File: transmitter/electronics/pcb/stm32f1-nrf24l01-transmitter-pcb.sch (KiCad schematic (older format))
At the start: 34 parts, among them K1 CONN_3, K10 CONN_3, K11 CONN_3, K12 UART, K2 CONN_3, K3 CONN_3, K4 CONN_3, K5 CONN_3, K6 CONN_3, K7 CONN_3, K8 CONN_3, K9 CONN_3, P1 Charge, P2 LED, P3 PWR-BAT, P4 PWR-IN, P5 Buzzer, P6 Meter, Q1 BC547B, SW1 ON/OFF, U1 LIPO_CHARGER_+_PROTECTION, U2 STM32F103C8T6_DEV_BOARD, U3 NRF24L01P

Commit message: Work on PCB
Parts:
- removed BT1: BATTERY, Pin_Headers:Pin_Header_Straight_1x02_Pitch2.54mm, symbol stm32f1-nrf24l01-transmitter-rescue:BATTERY
- removed P1: Charge, Pin_Headers:Pin_Header_Straight_1x02_Pitch2.54mm, symbol stm32f1-nrf24l01-transmitter-rescue:CONN_2
- removed P3: PWR-BAT, Pin_Headers:Pin_Header_Straight_1x02_Pitch2.54mm, symbol stm32f1-nrf24l01-transmitter-rescue:CONN_2
- removed P4: PWR-IN, Pin_Headers:Pin_Header_Straight_1x02_Pitch2.54mm, symbol stm32f1-nrf24l01-transmitter-rescue:CONN_2
- removed SW1: ON/OFF, Buttons_Switches_SMD:SW_SPST_FSMSM, symbol stm32f1-nrf24l01-transmitter-rescue:SPST
- added H1, H2: MountingHole, MountingHole:MountingHole_3.2mm_M3_DIN965, symbol Mechanical:MountingHole
- added J12: PB5, Connector_JST:JST_EH_B3B-EH-A_1x03_P2.50mm_Vertical, symbol stm32f1-nrf24l01-transmitter-rescue:CONN_3
- added J13: PB6, Connector_JST:JST_EH_B3B-EH-A_1x03_P2.50mm_Vertical, symbol stm32f1-nrf24l01-transmitter-rescue:CONN_3
- added J14: PB7, Connector_JST:JST_EH_B3B-EH-A_1x03_P2.50mm_Vertical, symbol stm32f1-nrf24l01-transmitter-rescue:CONN_3
- added J15: PB8, Connector_JST:JST_EH_B3B-EH-A_1x03_P2.50mm_Vertical, symbol stm32f1-nrf24l01-transmitter-rescue:CONN_3
- added J16: PB10, Connector_JST:JST_EH_B3B-EH-A_1x03_P2.50mm_Vertical, symbol stm32f1-nrf24l01-transmitter-rescue:CONN_3
- added J17: PB11, Connector_JST:JST_EH_B3B-EH-A_1x03_P2.50mm_Vertical, symbol stm32f1-nrf24l01-transmitter-rescue:CONN_3
- added J18: USB, Connector_JST:JST_EH_B4B-EH-A_1x04_P2.50mm_Vertical, symbol Connector_Generic:Conn_01x04
- added J19: BATTERY, Connector_JST:JST_EH_B2B-EH-A_1x02_P2.50mm_Vertical, symbol Connector_Generic:Conn_01x02
- added J21: SWITCH, Connector_JST:JST_EH_B2B-EH-A_1x02_P2.50mm_Vertical, symbol Connector_Generic:Conn_01x02
- added J22: NRF24 connector, Connector_JST:JST_EH_B7B-EH-A_1x07_P2.50mm_Vertical, symbol Connector_Generic:Conn_01x07
- added J26: Red, TestPoint:TestPoint_Pad_1.5x1.5mm, symbol Connector_Generic:Conn_01x01
- added J27: Blue, TestPoint:TestPoint_Pad_1.5x1.5mm, symbol Connector_Generic:Conn_01x01
- added J28: Charger LED, Connector_JST:JST_EH_B3B-EH-A_1x03_P2.50mm_Vertical, symbol Connector_Generic:Conn_01x03
- C1: renamed from C2; footprint Capacitors_SMD:C_0805_HandSoldering -> Capacitor_SMD:C_0805_2012Metric_Pad1.15x1.40mm_HandSolder
- C2: renamed from C3; footprint Capacitors_SMD:C_0805_HandSoldering -> Capacitor_SMD:C_0805_2012Metric_Pad1.15x1.40mm_HandSolder
- C3: renamed from C4; footprint Capacitors_SMD:C_0805_HandSoldering -> Capacitor_SMD:C_0805_2012Metric_Pad1.15x1.40mm_HandSolder
- C4: renamed from C1; footprint Capacitors_SMD:C_0805_HandSoldering -> Capacitor_SMD:C_0805_2012Metric_Pad1.15x1.40mm_HandSolder
- J1: renamed from K1; value CONN_3 -> PA1/A1; footprint Pin_Headers:Pin_Header_Straight_1x03_Pitch2.54mm -> Connector_JST:JST_EH_B3B-EH-A_1x03_P2.50mm_Vertical
- J10: renamed from K10; value CONN_3 -> PB3; footprint Pin_Headers:Pin_Header_Straight_1x03_Pitch2.54mm -> Connector_JST:JST_EH_B3B-EH-A_1x03_P2.50mm_Vertical
- J11: renamed from K11; value CONN_3 -> PB4; footprint Pin_Headers:Pin_Header_Straight_1x03_Pitch2.54mm -> Connector_JST:JST_EH_B3B-EH-A_1x03_P2.50mm_Vertical
- J2: renamed from K2; value CONN_3 -> PA2/A2; footprint Pin_Headers:Pin_Header_Straight_1x03_Pitch2.54mm -> Connector_JST:JST_EH_B3B-EH-A_1x03_P2.50mm_Vertical
- J20: renamed from K12; footprint Pin_Headers:Pin_Header_Straight_1x03_Pitch2.54mm -> Connector_PinHeader_2.54mm:PinHeader_1x03_P2.54mm_Vertical; symbol stm32f1-nrf24l01-transmitter-rescue:CONN_3 -> Connector_Generic:Conn_01x03
- J23: renamed from P5; footprint Pin_Headers:Pin_Header_Straight_1x02_Pitch2.54mm -> Connector_JST:JST_EH_B2B-EH-A_1x02_P2.50mm_Vertical; symbol stm32f1-nrf24l01-transmitter-rescue:CONN_2 -> Connector_Generic:Conn_01x02
- J24: renamed from P6; footprint Pin_Headers:Pin_Header_Straight_1x02_Pitch2.54mm -> Connector_JST:JST_EH_B2B-EH-A_1x02_P2.50mm_Vertical; symbol stm32f1-nrf24l01-transmitter-rescue:CONN_2 -> Connector_Generic:Conn_01x02
- J25: renamed from P2; footprint Pin_Headers:Pin_Header_Straight_1x02_Pitch2.54mm -> Connector_JST:JST_EH_B2B-EH-A_1x02_P2.50mm_Vertical; symbol stm32f1-nrf24l01-transmitter-rescue:CONN_2 -> Connector_Generic:Conn_01x02
- J3: renamed from K3; value CONN_3 -> PA3/A3; footprint Pin_Headers:Pin_Header_Straight_1x03_Pitch2.54mm -> Connector_JST:JST_EH_B3B-EH-A_1x03_P2.50mm_Vertical
- J4: renamed from K4; value CONN_3 -> PA4/A4; footprint Pin_Headers:Pin_Header_Straight_1x03_Pitch2.54mm -> Connector_JST:JST_EH_B3B-EH-A_1x03_P2.50mm_Vertical
- J5: renamed from K5; value CONN_3 -> PA5/A5; footprint Pin_Headers:Pin_Header_Straight_1x03_Pitch2.54mm -> Connector_JST:JST_EH_B3B-EH-A_1x03_P2.50mm_Vertical
- J6: renamed from K6; value CONN_3 -> PA6/A6; footprint Pin_Headers:Pin_Header_Straight_1x03_Pitch2.54mm -> Connector_JST:JST_EH_B3B-EH-A_1x03_P2.50mm_Vertical
- J7: renamed from K7; value CONN_3 -> PA7/A7; footprint Pin_Headers:Pin_Header_Straight_1x03_Pitch2.54mm -> Connector_JST:JST_EH_B3B-EH-A_1x03_P2.50mm_Vertical
- J8: renamed from K8; value CONN_3 -> PB0/A8; footprint Pin_Headers:Pin_Header_Straight_1x03_Pitch2.54mm -> Connector_JST:JST_EH_B3B-EH-A_1x03_P2.50mm_Vertical
- J9: renamed from K9; value CONN_3 -> PB1/A9; footprint Pin_Headers:Pin_Header_Straight_1x03_Pitch2.54mm -> Connector_JST:JST_EH_B3B-EH-A_1x03_P2.50mm_Vertical
- Q1: footprint TO_SOT_Packages_THT:TO-92_Inline_Wide -> Package_TO_SOT_SMD:SOT-23_Handsoldering
- R1: renamed from R2; footprint Resistors_SMD:R_0805_HandSoldering -> Resistor_SMD:R_0805_2012Metric_Pad1.15x1.40mm_HandSolder
- R2: renamed from R3; footprint Resistors_SMD:R_0805_HandSoldering -> Resistor_SMD:R_0805_2012Metric_Pad1.15x1.40mm_HandSolder
- R3: renamed from R4; footprint Resistors_SMD:R_0805_HandSoldering -> Resistor_SMD:R_0805_2012Metric_Pad1.15x1.40mm_HandSolder
- R4: renamed from R5; footprint Resistors_SMD:R_0805_HandSoldering -> Resistor_SMD:R_0805_2012Metric_Pad1.15x1.40mm_HandSolder
- R5: renamed from R1; footprint Resistors_SMD:R_0805_HandSoldering -> Resistor_SMD:R_0805_2012Metric_Pad1.15x1.40mm_HandSolder
- SP1: footprint Buzzers_Beepers:Buzzer_12x9.5RM7.6 -> Buzzer_Beeper:Buzzer_12x9.5RM7.6
- U2: footprint WLA:STM32F103C8T6 -> WLA:STM32F103C8T6_DEV_BOARD
- U3: footprint WLA:NRF24L01P-PA-LNA -> Connector_PinHeader_2.54mm:PinHeader_2x04_P2.54mm_Vertical
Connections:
- net BUZZER: now also R3.2; no longer R3.1
- net CSN: now also J22.3 (Pin_3)
- net GND: now also J12.1 (P1), J13.1 (P1), J14.1 (P1), J15.1 (P1), J16.1 (P1), J17.1 (P1), J18.1 (Pin_1), J22.1 (Pin_1)
- net IRQ: now also J22.5 (Pin_5)
- net MISO: now also J22.6 (Pin_6)
- net MOSI: now also J22.4 (Pin_4)
- net PB10: now also J16.3 (P3); no longer J11.3 (P3)
- net PB11: now also J17.3 (P3); no longer J10.3 (P3)
- net PB3: now also J10.3 (P3)
- net PB4: now also J11.3 (P3)
- net PB5: now also J12.3 (P3)
- net PB6: now also J13.3 (P3)
- net PB7: now also J14.3 (P3)
- net PB8: now also J15.3 (P3)
- net RX: now also J20.3 (Pin_3); no longer J20.2 (PM)
- net SCK: now also J22.7 (Pin_7)
- net TX: now also J20.2 (Pin_2); no longer J20.3 (P3)
- net VCC: now also J12.2 (PM), J13.2 (PM), J14.2 (PM), J15.2 (PM), J16.2 (PM), J17.2 (PM), J22.2 (Pin_2)
- net VDD: now also J21.2 (Pin_2)
- net USBDM: now reaches U2.8 (PA11/USBDM)
- net USBDM: now also J18.3 (Pin_3)
- net USBDP: now reaches U2.9 (PA12/USBDP)
- net USBDP: now also J18.2 (Pin_2)
- net at U1.1 (LiPo+): now also J19.2 (Pin_2)
- net at U1.2 (LiPo-): now also J19.1 (Pin_1)
- net at U1.3 (OUT+): now also J21.1 (Pin_1)
- net +USB: now reaches U1.5 (USB+)
- net +USB: now also J18.4 (Pin_4), J28.3 (Pin_3)
- net at Q1.2 (B): now also R3.1; no longer R3.2
- net PB9 renamed METER
- new net: J27.1 (Pin_1), J28.1 (Pin_1)
- new net: J26.1 (Pin_1), J28.2 (Pin_2)
- no-connect marks 11 -> 3
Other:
- note added: "Note that 4 pins of J22 and U3 are \nmade to overlap, so that we can save \nspace since we only want one \noption ever"
- note added: "USB"
- moved on the sheet: C1, C2, C3, C4, Q1, R1, R2, R3, R4, R5, SP1, U1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

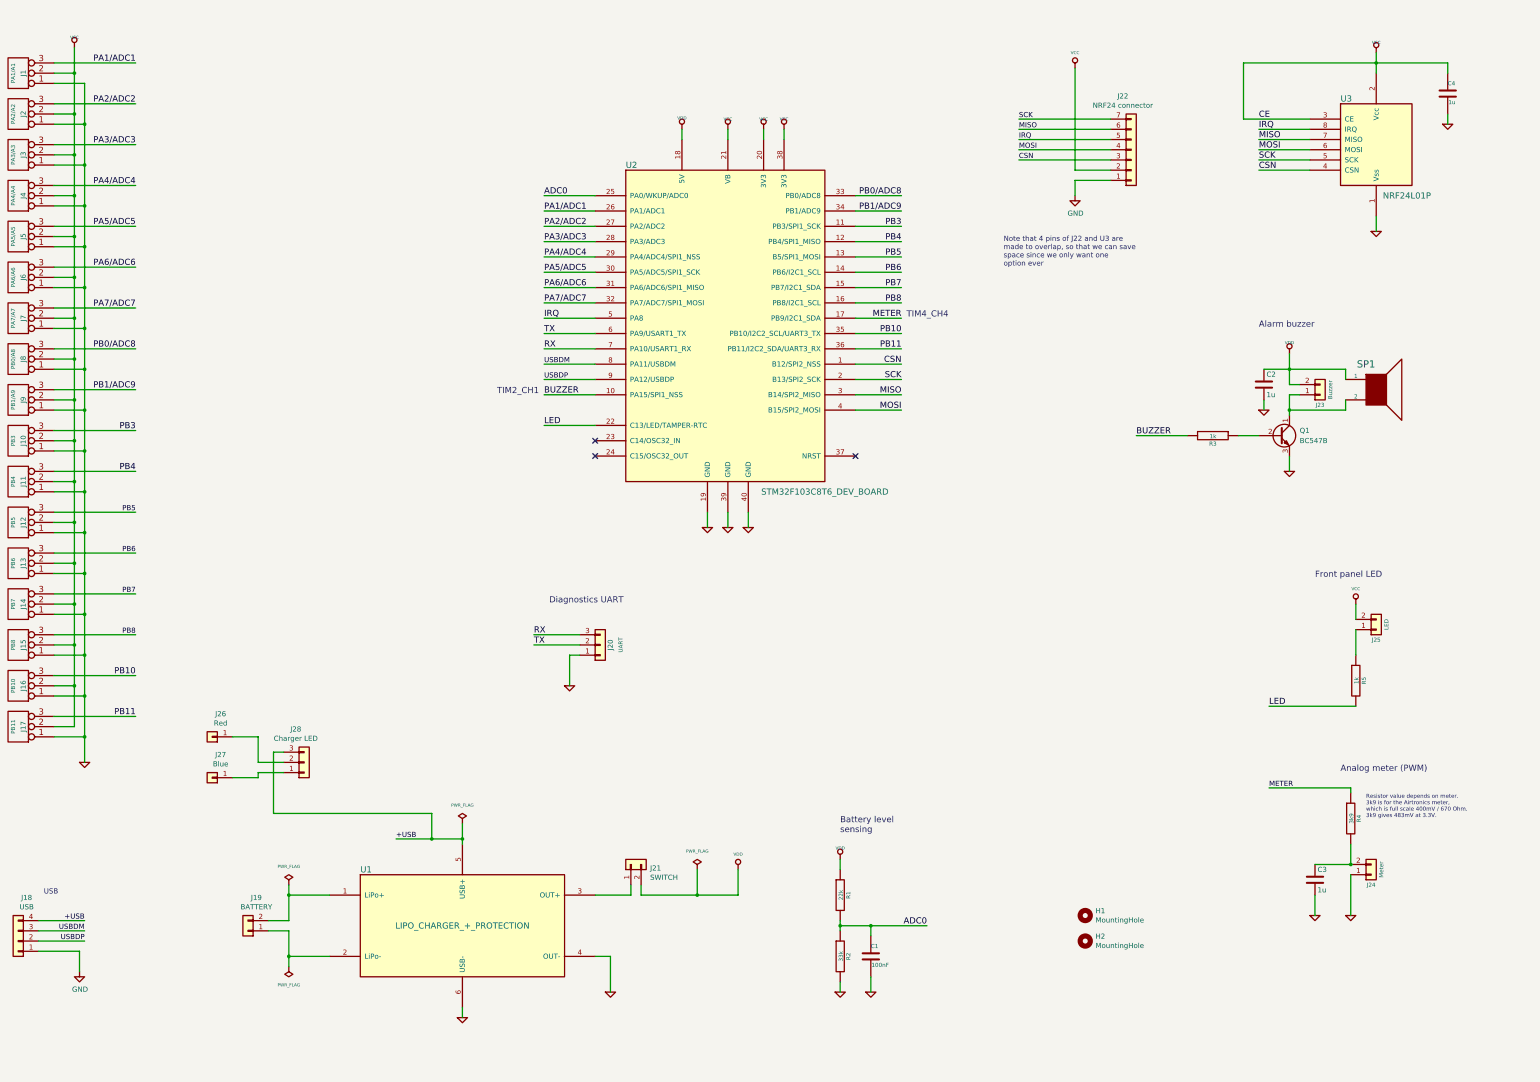
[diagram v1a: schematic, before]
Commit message: Update PCB without Blue Pill, but use STM32F103 directly
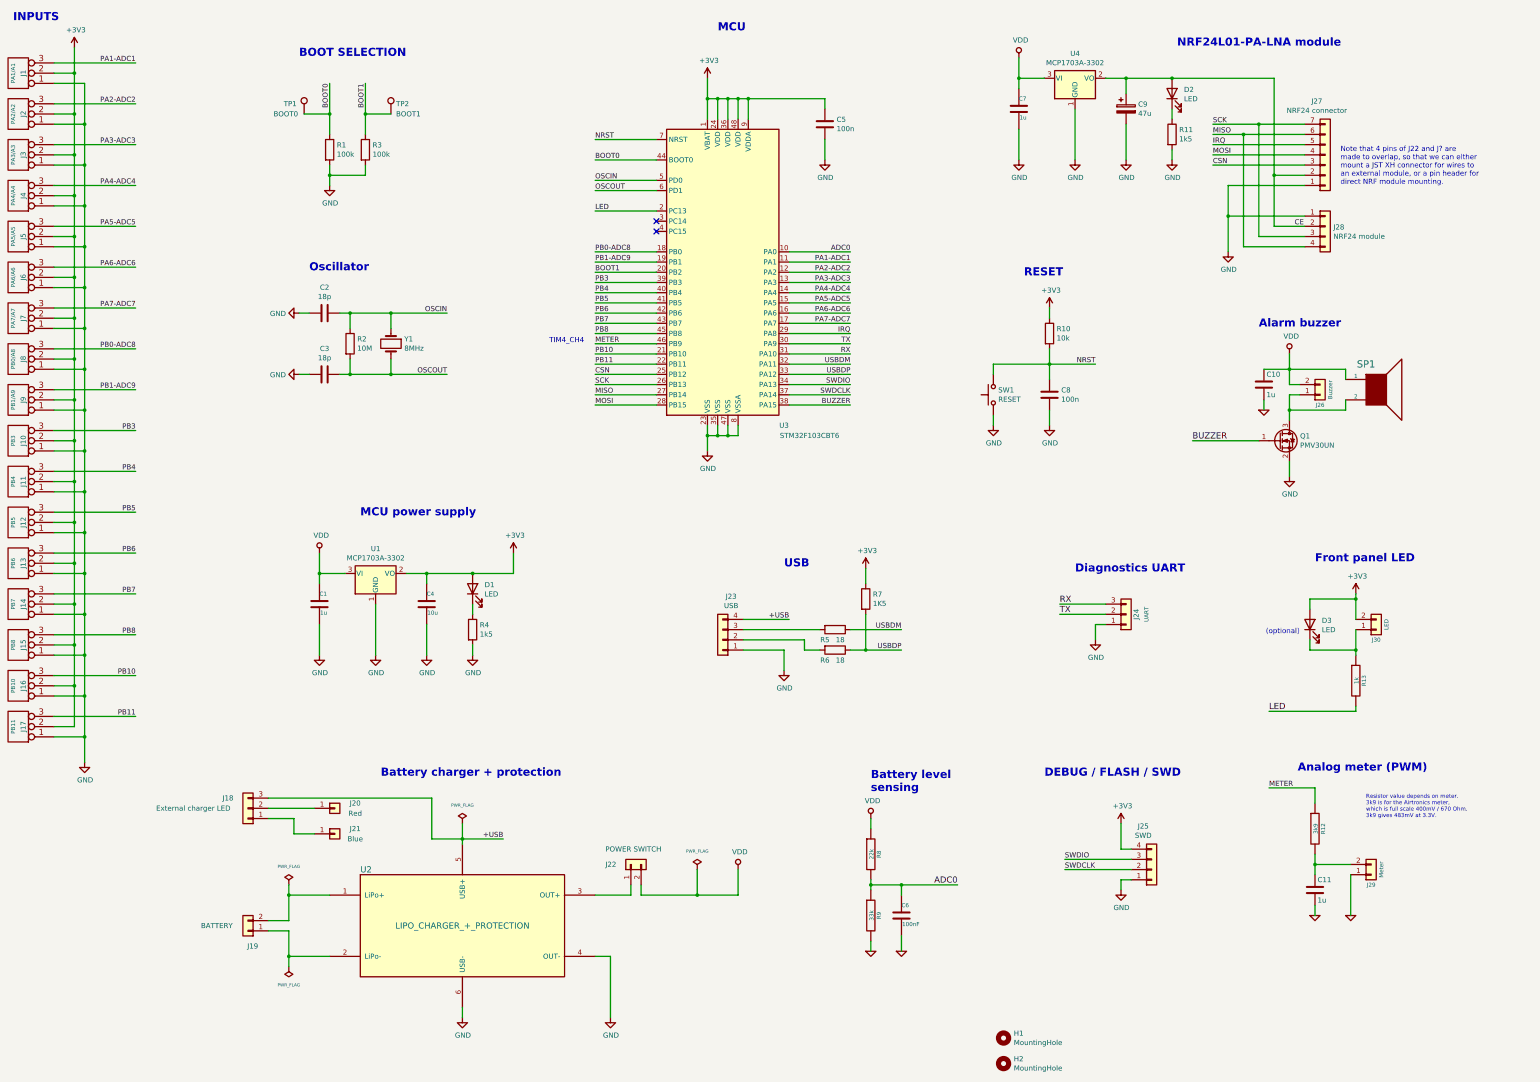
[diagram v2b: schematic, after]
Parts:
- removed Q1: BC547B, Package_TO_SOT_SMD:SOT-23_Handsoldering, symbol stm32f1-nrf24l01-transmitter-rescue:Q_NPN_CBE
- removed R3: 1k, Resistor_SMD:R_0805_2012Metric_Pad1.15x1.40mm_HandSolder, symbol stm32f1-nrf24l01-transmitter-rescue:R-RESCUE-stm32f1-nrf24l01-transmitter
- removed U2: STM32F103C8T6_DEV_BOARD, WLA:STM32F103C8T6_DEV_BOARD, symbol stm32f1-nrf24l01-transmitter-rescue:STM32F103C8T6_DEV_BOARD
- removed U3: NRF24L01P, Connector_PinHeader_2.54mm:PinHeader_2x04_P2.54mm_Vertical, symbol stm32f1-nrf24l01-transmitter-rescue:NRF24L01P
- added C1, C7: 1u, Capacitor_SMD:C_0805_2012Metric_Pad1.15x1.40mm_HandSolder, symbol stm32f1-nrf24l01-transmitter-rescue:C-RESCUE-stm32f1-nrf24l01-transmitter
- added C2, C3: 18p, Capacitor_SMD:C_0603_1608Metric_Pad1.05x0.95mm_HandSolder, symbol Device:C
- added C5, C8: 100n, Capacitor_SMD:C_0603_1608Metric_Pad1.05x0.95mm_HandSolder, symbol Device:C
- added C9: 47u, Capacitor_SMD:C_0805_2012Metric_Pad1.15x1.40mm_HandSolder, symbol Device:CP
- added D1, D2, D3: LED, LED_SMD:LED_0805_2012Metric_Pad1.15x1.40mm_HandSolder, symbol Device:LED
- added J25: SWD, Connector_PinHeader_2.54mm:PinHeader_1x04_P2.54mm_Vertical, symbol Connector_Generic:Conn_01x04
- added J28: NRF24 module, Connector_PinHeader_2.54mm:PinHeader_1x04_P2.54mm_Vertical, symbol Connector_Generic:Conn_01x04
- added Q1: PMV30UN, Package_TO_SOT_SMD:SOT-23, symbol Transistor_FET:BSS138
- added R1, R3: 100k, Resistor_SMD:R_0805_2012Metric_Pad1.15x1.40mm_HandSolder, symbol Device:R
- added R10: 10k, Resistor_SMD:R_0805_2012Metric_Pad1.15x1.40mm_HandSolder, symbol Device:R
- added R11, R4: 1k5, Resistor_SMD:R_0805_2012Metric_Pad1.15x1.40mm_HandSolder, symbol Device:R
- added R2: 10M, Resistor_SMD:R_0805_2012Metric_Pad1.15x1.40mm_HandSolder, symbol Device:R
- added R5, R6: 18, Resistor_SMD:R_0805_2012Metric_Pad1.15x1.40mm_HandSolder, symbol Device:R
- added R7: 1K5, Resistor_SMD:R_0805_2012Metric_Pad1.15x1.40mm_HandSolder, symbol Device:R
- added SW1: RESET, tact-switch:Tact switch 6x4x3, symbol Switch:SW_Push
- added TP1: BOOT0, TestPoint:TestPoint_Pad_1.5x1.5mm, symbol Connector:TestPoint
- added TP2: BOOT1, TestPoint:TestPoint_Pad_1.5x1.5mm, symbol Connector:TestPoint
- added U1, U4: MCP1703A-3302, Package_TO_SOT_SMD:SOT-23, symbol Regulator_Linear:MCP1703A-3302_SOT23
- added U3: STM32F103CBT6, Package_QFP:LQFP-48_7x7mm_P0.5mm, symbol MCU_ST_STM32F1:STM32F103CBTx
- added Y1: 8MHz, Crystal:Crystal_SMD_5032-2Pin_5.0x3.2mm_HandSoldering, symbol Device:Crystal
- C4: value 1u -> 10u
- J1, J10, J11, J12, J13, J14, J15, J16, J17, J2, J3, J4, J5, J6, J7, J8, J9: footprint Connector_JST:JST_EH_B3B-EH-A_1x03_P2.50mm_Vertical -> Connector_JST:JST_XH_B3B-XH-A_1x03_P2.50mm_Vertical
- J18: renamed from J28; value Charger LED -> External charger LED; footprint Connector_JST:JST_EH_B3B-EH-A_1x03_P2.50mm_Vertical -> Connector_JST:JST_XH_B3B-XH-A_1x03_P2.50mm_Vertical
- J19: footprint Connector_JST:JST_EH_B2B-EH-A_1x02_P2.50mm_Vertical -> Connector_JST:JST_XH_B2B-XH-A_1x02_P2.50mm_Vertical
- J22: renamed from J21; value SWITCH -> POWER SWITCH; footprint Connector_JST:JST_EH_B2B-EH-A_1x02_P2.50mm_Vertical -> Connector_JST:JST_XH_B2B-XH-A_1x02_P2.50mm_Vertical
- J23: renamed from J18; footprint Connector_JST:JST_EH_B4B-EH-A_1x04_P2.50mm_Vertical -> Connector_JST:JST_XH_B4B-XH-A_1x04_P2.50mm_Vertical
- J26: renamed from J23; footprint Connector_JST:JST_EH_B2B-EH-A_1x02_P2.50mm_Vertical -> Connector_JST:JST_XH_B2B-XH-A_1x02_P2.50mm_Vertical
- J27: renamed from J22; footprint Connector_JST:JST_EH_B7B-EH-A_1x07_P2.50mm_Vertical -> Connector_JST:JST_XH_B7B-XH-A_1x07_P2.50mm_Vertical
- J29: renamed from J24; footprint Connector_JST:JST_EH_B2B-EH-A_1x02_P2.50mm_Vertical -> Connector_JST:JST_XH_B2B-XH-A_1x02_P2.50mm_Vertical
- J30: renamed from J25; footprint Connector_JST:JST_EH_B2B-EH-A_1x02_P2.50mm_Vertical -> Connector_JST:JST_XH_B2B-XH-A_1x02_P2.50mm_Vertical
- renumbered C2 to C10, C3 to C11, C1 to C6, J26 to J20, J27 to J21, J20 to J24, R4 to R12, R5 to R13, R1 to R8, R2 to R9, U1 to U2
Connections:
- net ADC0: now also U3.10 (PA0)
- net BUZZER: now also Q1.1 (G), U3.38 (PA15)
- net CSN: now also U3.25 (PB12)
- net GND: now also C1.2, C2.2, C3.2, C5.2, C7.2, C8.2, C9.2, J25.1 (Pin_1), J28.1 (Pin_1), Q1.2 (S), R1.2, R11.2, R3.2, R4.2, SW1.1, U1.1 (GND), U3.23 (VSS), U3.35 (VSS), U3.47 (VSS), U3.8 (VSSA), U4.1 (GND)
- net IRQ: now also U3.29 (PA8)
- net LED: now also U3.2 (PC13)
- net METER: now also U3.46 (PB9)
- net MISO: now also J28.4 (Pin_4), U3.27 (PB14)
- net MOSI: now also U3.28 (PB15)
- net PB10: now also U3.21 (PB10)
- net PB11: now also U3.22 (PB11)
- net PB3: now also U3.39 (PB3)
- net PB4: now also U3.40 (PB4)
- net PB5: now also U3.41 (PB5)
- net PB6: now also U3.42 (PB6)
- net PB7: now also U3.43 (PB7)
- net PB8: now also U3.45 (PB8)
- net RX: now also U3.31 (PA10)
- net SCK: now also J28.3 (Pin_3), U3.26 (PB13)
- net TX: now also U3.30 (PA9)
- net USBDM: now also R5.1, U3.32 (PA11); no longer J23.3 (Pin_3)
- net USBDP: now also R6.1, R7.2, U3.33 (PA12); no longer J23.2 (Pin_2)
- net VDD: now also C1.1, C7.1, U1.3 (VI), U4.3 (VI)
- net at J30.1 (Pin_1), R13.1: now also D3.1 (K)
- net at J26.1 (Pin_1), SP1.2: now also Q1.3 (D)
- net PA1/ADC1 renamed PA1-ADC1
- net PA1-ADC1: now also U3.11 (PA1)
- net PA2/ADC2 renamed PA2-ADC2
- net PA2-ADC2: now also U3.12 (PA2)
- net PA3/ADC3 renamed PA3-ADC3
- net PA3-ADC3: now also U3.13 (PA3)
- net PA4/ADC4 renamed PA4-ADC4
- net PA4-ADC4: now also U3.14 (PA4)
- net PA5/ADC5 renamed PA5-ADC5
- net PA5-ADC5: now also U3.15 (PA5)
- net PA6/ADC6 renamed PA6-ADC6
- net PA6-ADC6: now also U3.16 (PA6)
- net PA7/ADC7 renamed PA7-ADC7
- net PA7-ADC7: now also U3.17 (PA7)
- net PB0/ADC8 renamed PB0-ADC8
- net PB0-ADC8: now also U3.18 (PB0)
- net PB1/ADC9 renamed PB1-ADC9
- net PB1-ADC9: now also U3.19 (PB1)
- net VCC renamed +3V3
- net +3V3: now also C5.1, D1.2 (A), D3.2 (A), J25.4 (Pin_4), R10.1, R7.1, U1.2 (VO), U3.1 (VBAT), U3.24 (VDD), U3.36 (VDD), U3.48 (VDD), U3.9 (VDDA); no longer J27.2 (Pin_2)
- new net: J23.2 (Pin_2), R6.2
- new net: J23.3 (Pin_3), R5.2
- new net: D2.1 (K), R11.1
- new net: D1.1 (K), R4.1
- new net BOOT0: R1.1, TP1.1, U3.44 (BOOT0)
- new net BOOT1: R3.1, TP2.1, U3.20 (PB2)
- new net CE: C9.1, D2.2 (A), J27.2 (Pin_2), J28.2 (Pin_2), U4.2 (VO)
- new net NRST: C8.1, R10.2, SW1.2, U3.7 (NRST)
- new net OSCIN: C2.1, R2.1, U3.5 (PD0), Y1.1
- new net OSCOUT: C3.1, R2.2, U3.6 (PD1), Y1.2
- new net SWDCLK: J25.2 (Pin_2), U3.37 (PA14)
- new net SWDIO: J25.3 (Pin_3), U3.34 (PA13)
- no-connect marks 3 -> 2
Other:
- note added: "(optional)"
- note added: "BOOT SELECTION"
- note added: "Battery charger + protection"
- note added: "DEBUG / FLASH / SWD"
- note added: "INPUTS"
- note added: "MCU"
- note added: "MCU power supply"
- note added: "NRF24L01-PA-LNA module"
- note added: "Note that 4 pins of J22 and J? are \nmade to overlap, so that we can either\nmount a JST XH connector for wires to\nan external module, or a pin header for \ndirect NRF module mounting."
- note added: "Oscillator"
- note added: "RESET"
- note removed: "Note that 4 pins of J22 and U3 are \nmade to overlap, so that we can save \nspace since we only want one \noption ever"
- note removed: "TIM2_CH1"
- moved on the sheet: C11, C6, H1, H2, J18, J20, J21, J23, J24, J27, R12, R8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
